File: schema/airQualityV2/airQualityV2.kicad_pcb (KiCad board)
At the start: 2 copper layers, 47.6 x 51.4 mm, 17 parts, among them J1 mhz19, J2 ccs811, J3 Conn_01x04_Female, U1 ESP32_DevKit_V1_DOIT

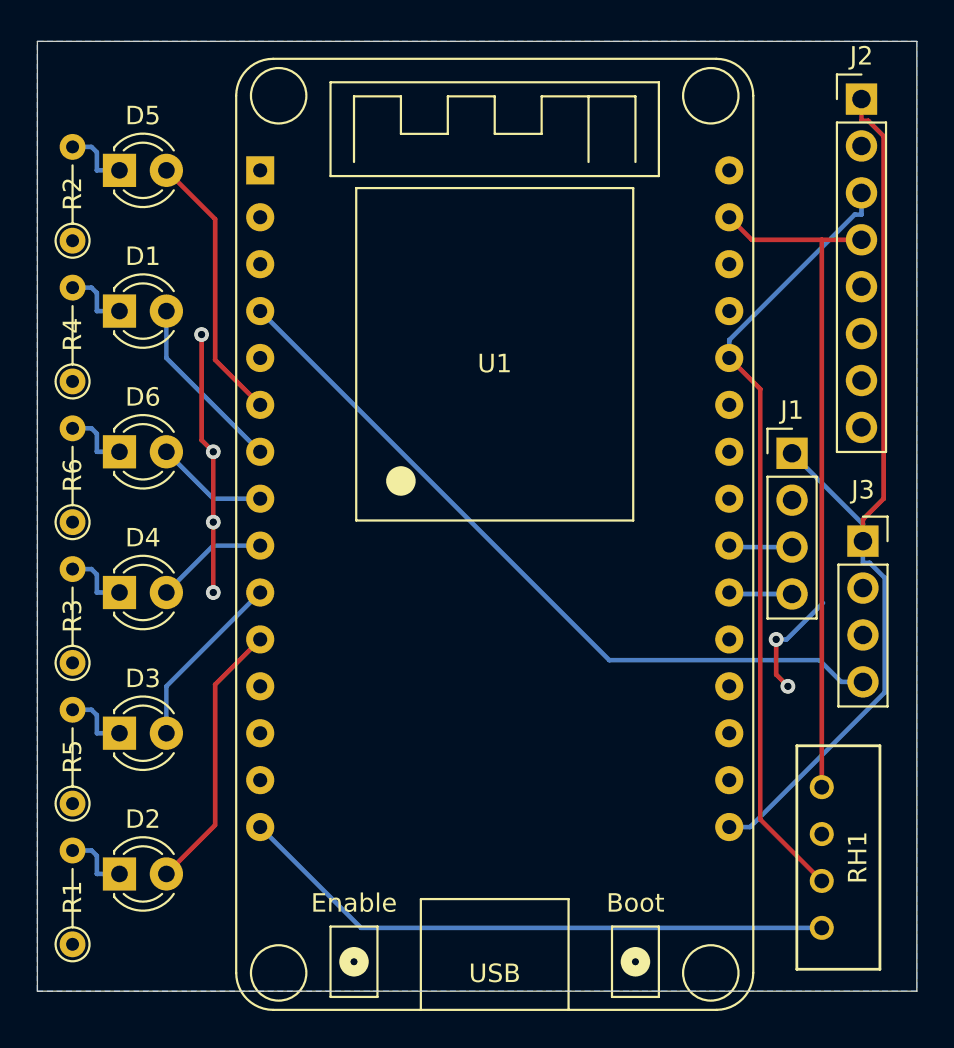
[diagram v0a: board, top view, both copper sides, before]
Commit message: update schematic
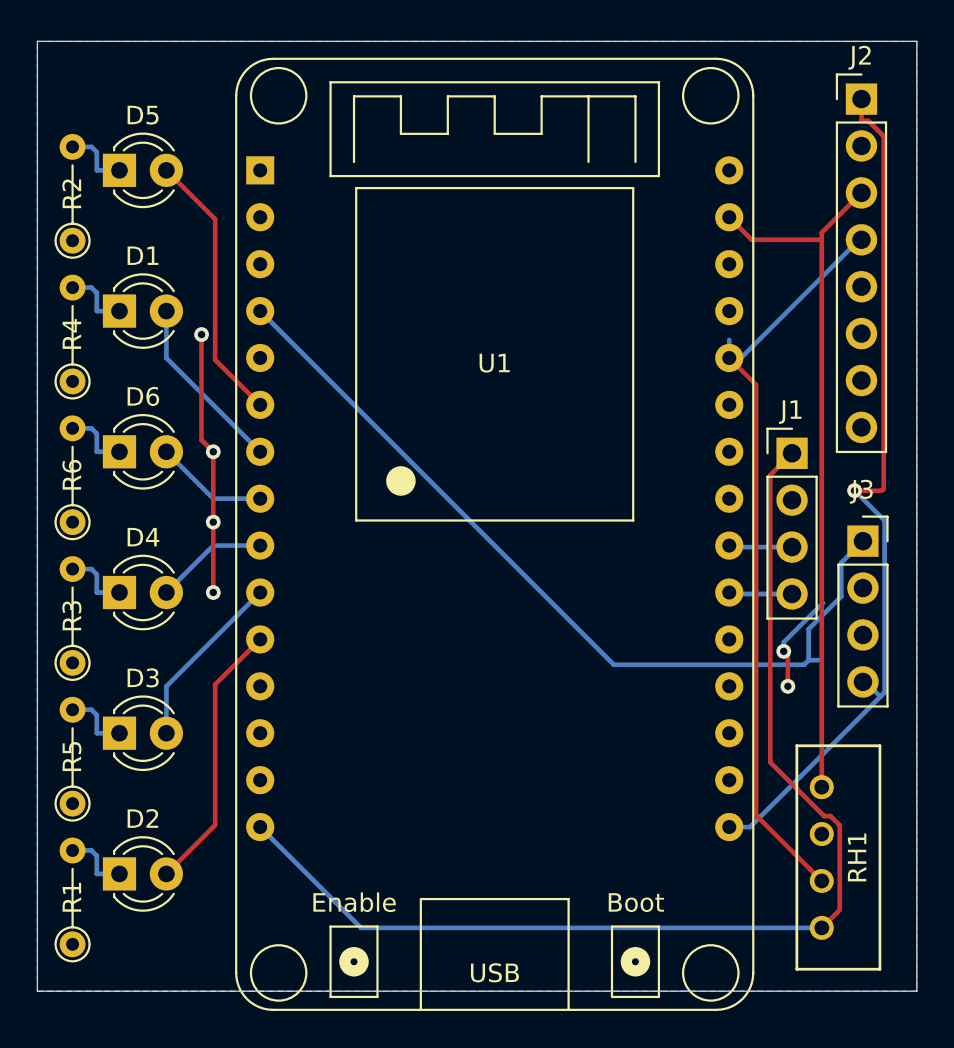
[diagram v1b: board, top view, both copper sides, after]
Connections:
- J1 pad 1: +3V3 -> +5V
- J2 pad 3: sda -> scl
- J2 pad 4: scl -> sda
- J2 pad 5: Net-(J2-Pad5) -> GND
- J3 pad 1: +3V3 -> MQ7A
- J3 pad 2: GND -> Net-(J3-Pad2)
- J3 pad 3: Net-(J3-Pad3) -> GND
- J3 pad 4: MQ7A -> +3V3
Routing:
- net +5V: track 32.7 -> 61.0 mm
- net MQ7A: track 41.0 -> 45.5 mm
- net +3V3: track 51.8 -> 47.7 mm, vias 0 -> 1
- net sda: track 42.5 -> 41.0 mm
- net scl: track 37.3 -> 38.6 mm
- net GND: track 20.4 -> 19.7 mm
